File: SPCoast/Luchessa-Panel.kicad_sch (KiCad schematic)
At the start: 21 parts, among them SW8784 783, SW8796 795, SW8800 799, U8004 0x24, U8005 0x25, U8006 0x26

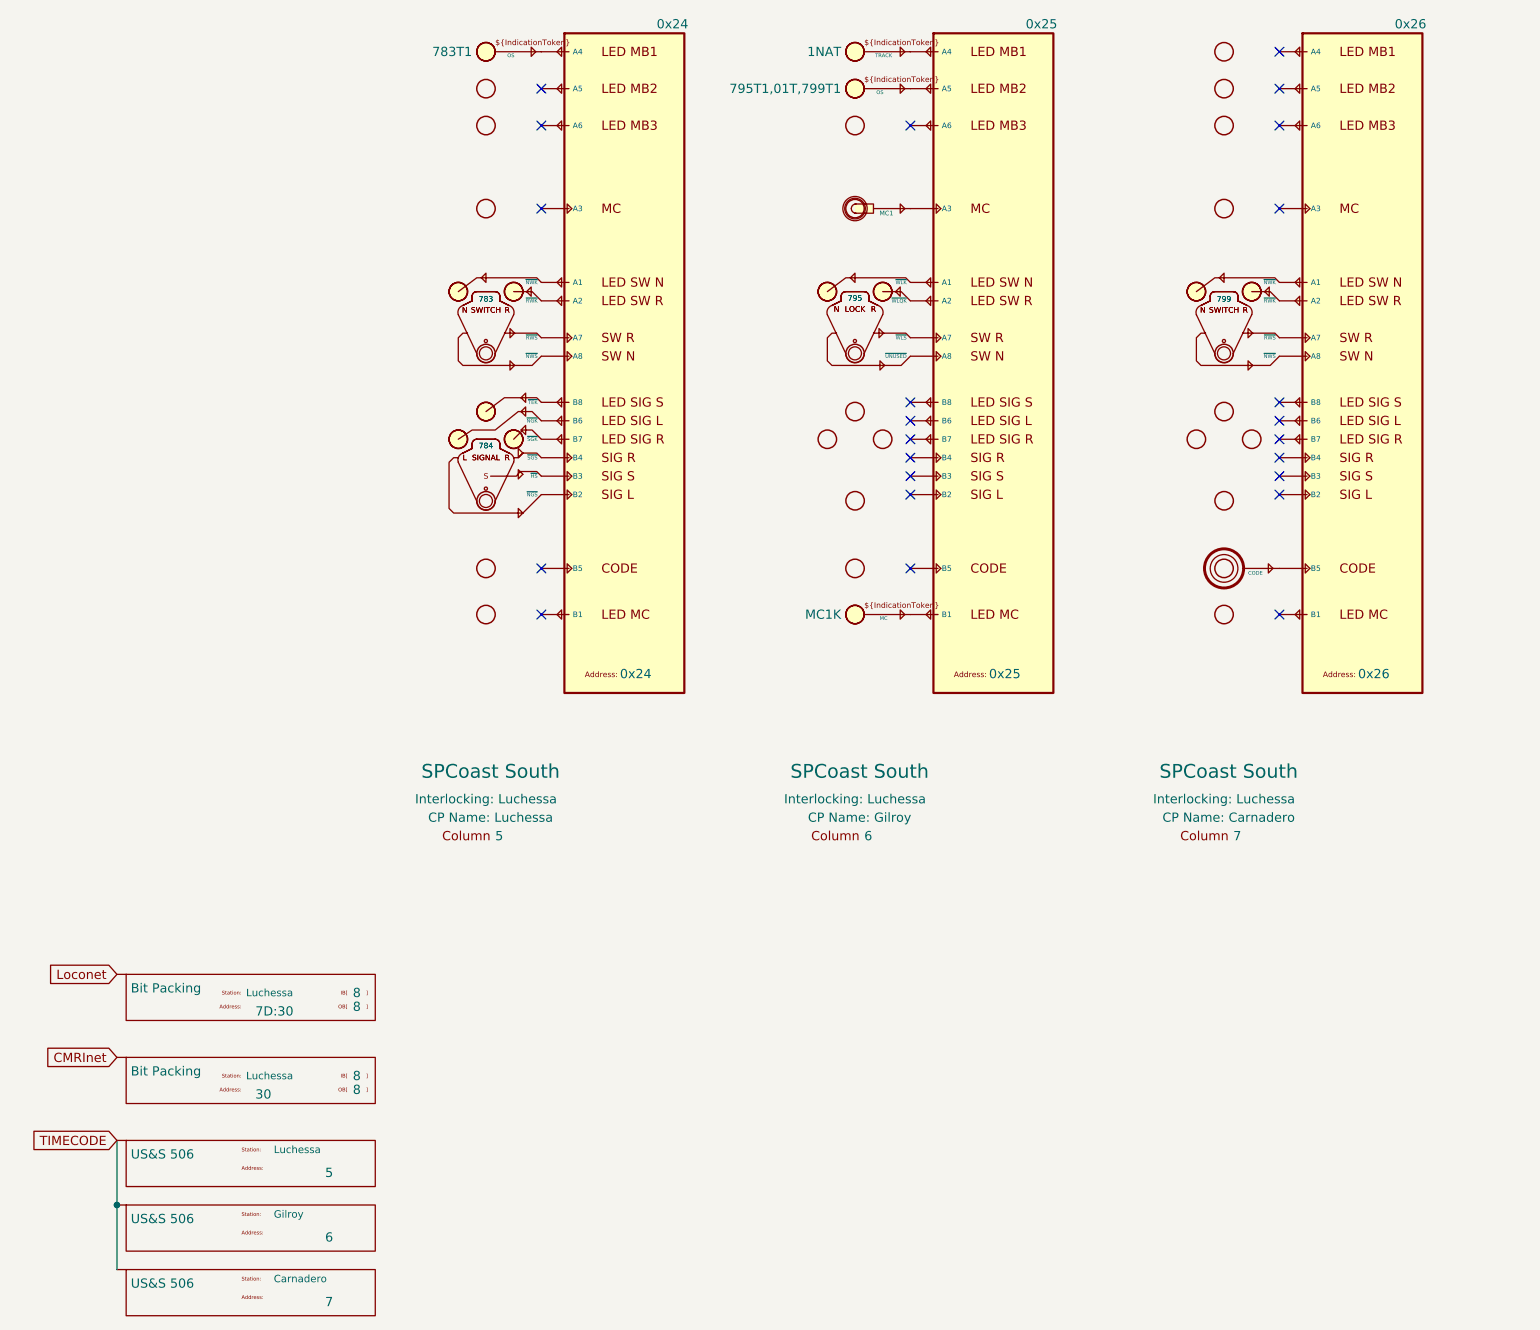
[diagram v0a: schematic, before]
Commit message: chore(kicad): owner mockup: explicit seam wiring on Luchessa and South-cTc, host and bus pins
Owner's edits, committed as they stand (2026-10-21), before scripted edits build on them.

- Interlocking gains Codeline and Host pins; MAIN HOUSE's Interlocking pin is Codeline.
- OfficeUnit gains Host and Codeline pins; JohnCTC desk processor drawn on South-cTc.
- Processor gains Transport and IO pins; MAX7313 and MCP23017 gain an I2C bus pin.
- Transports: Codeline pin renamed Host; JMRI_MQTT instance added; Loconet removed.
- Encodings' pin renamed Transport; Luchessa's 506 and Bit Packing instances removed.
- SPCoastApp virtual host (FieldUnit_Virtual) hosts CMRInet and JMRI_MQTT.
- Luchessa: unit, houses and Time Coded on one net; Host to its own processor;
  panel MAX7313s on the desk bus (OfficeBus).
- Watsonville, Caltrain, Interchange: first-pass Processor placeholders, to be redrawn.

Verified: netlist and ERC exported from the saved project; field diff against the
committed netlist shows no per-instance field lost.
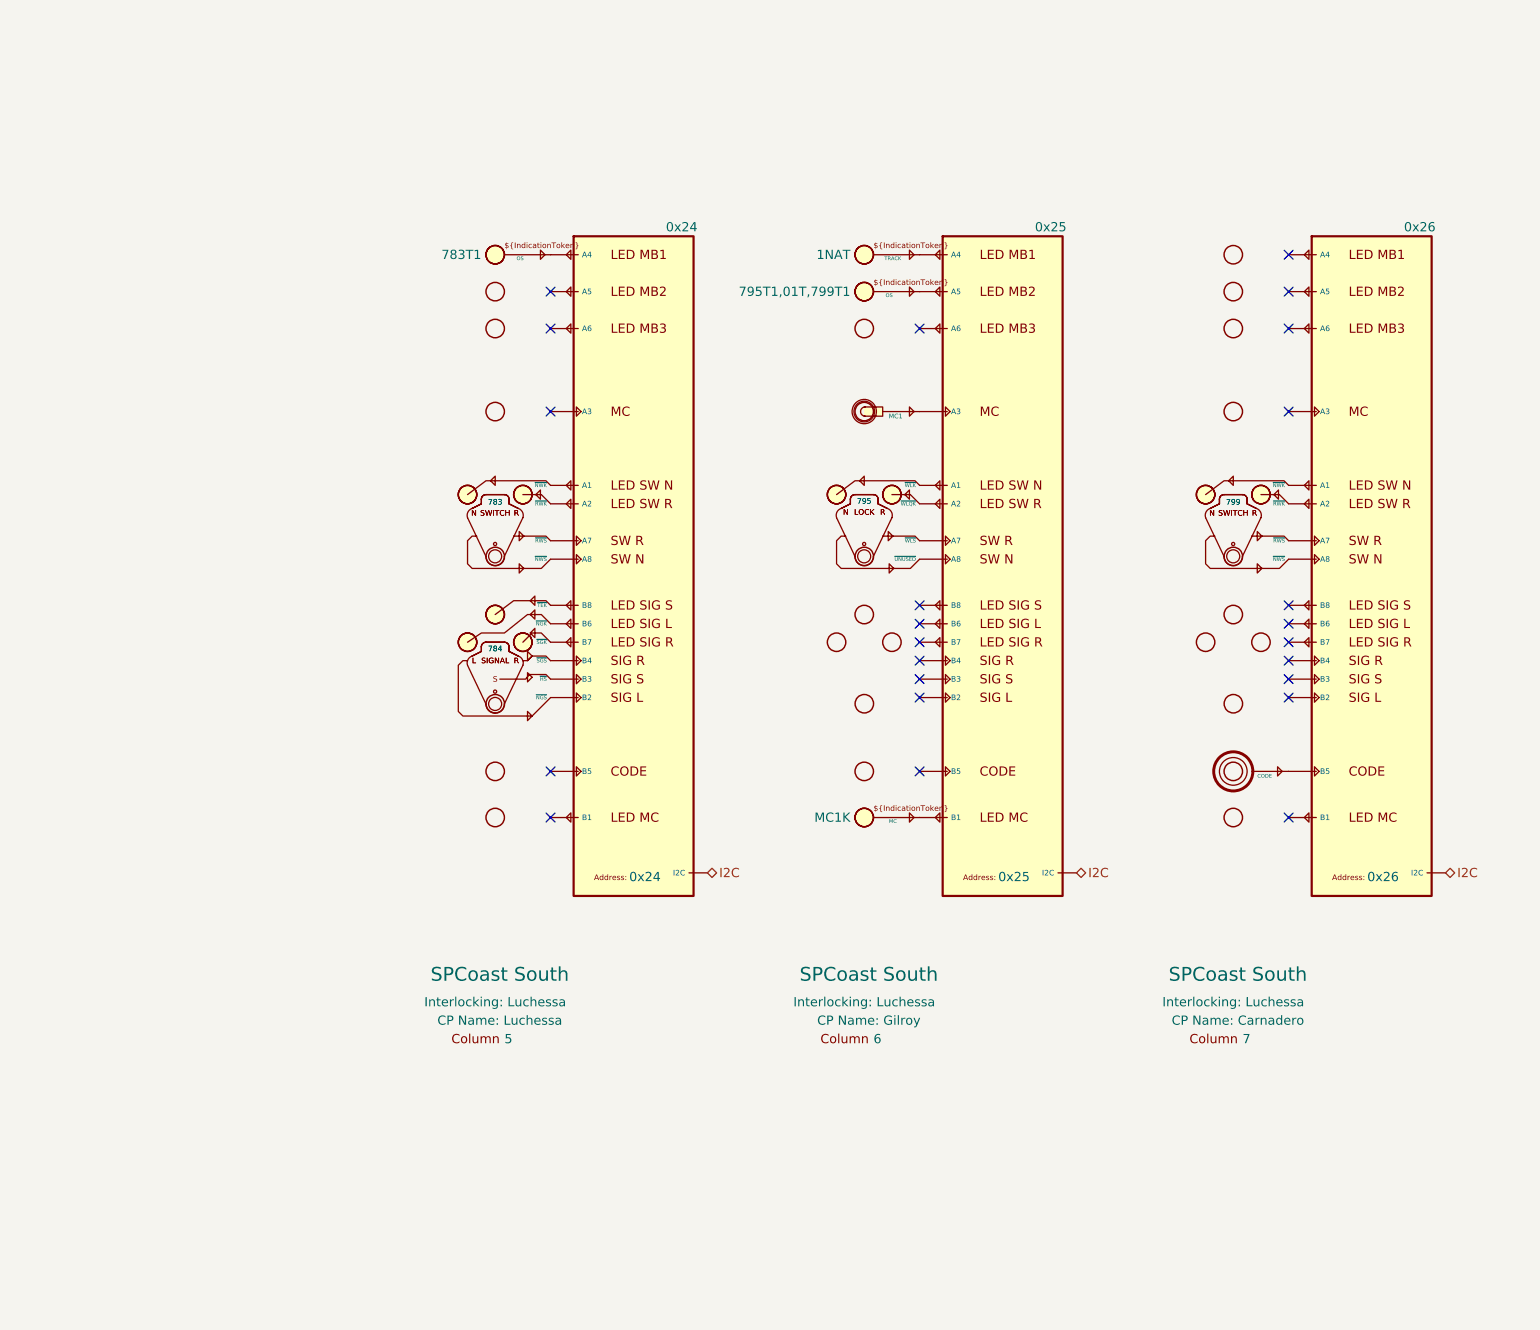
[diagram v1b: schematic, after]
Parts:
- removed Encoding8002, Encoding8003, Encoding8004: US&S 506, symbol Railroad-Office:Codeline-Encoding-US&S-506
- removed Encoding8005, Encoding8006: Bit Packing, symbol Railroad-Office:Codeline-Encoding-Bits
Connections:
- new net I2C: U8004.17 (I2C), U8005.17 (I2C), U8006.17 (I2C)

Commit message: chore(kicad): owner edits: Remote-IO node fields (Kind CMRI / MQTT-JMRI, bytes, UA), Interlocking Name, IOBus pins on remote drivers, sheet cleanup
Owner's edits of 2026-10-22, committed as they stand before the read-back.
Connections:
- net I2C renamed IOBus
